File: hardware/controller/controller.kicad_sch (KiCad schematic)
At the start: 0 parts

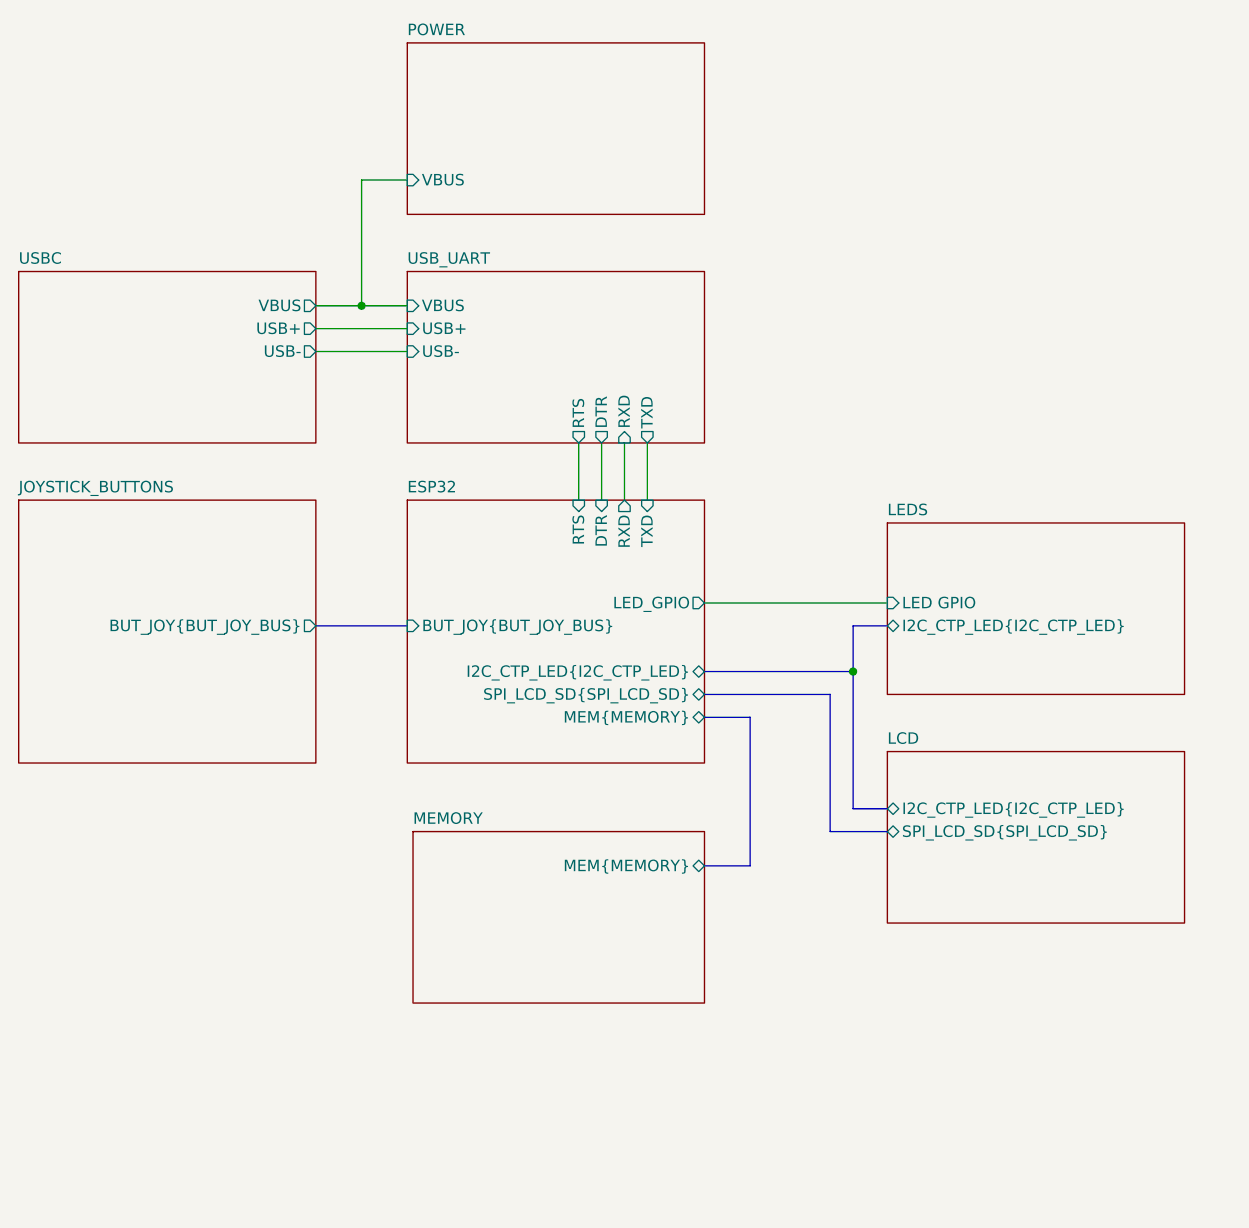
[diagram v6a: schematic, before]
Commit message: modified power circuitry
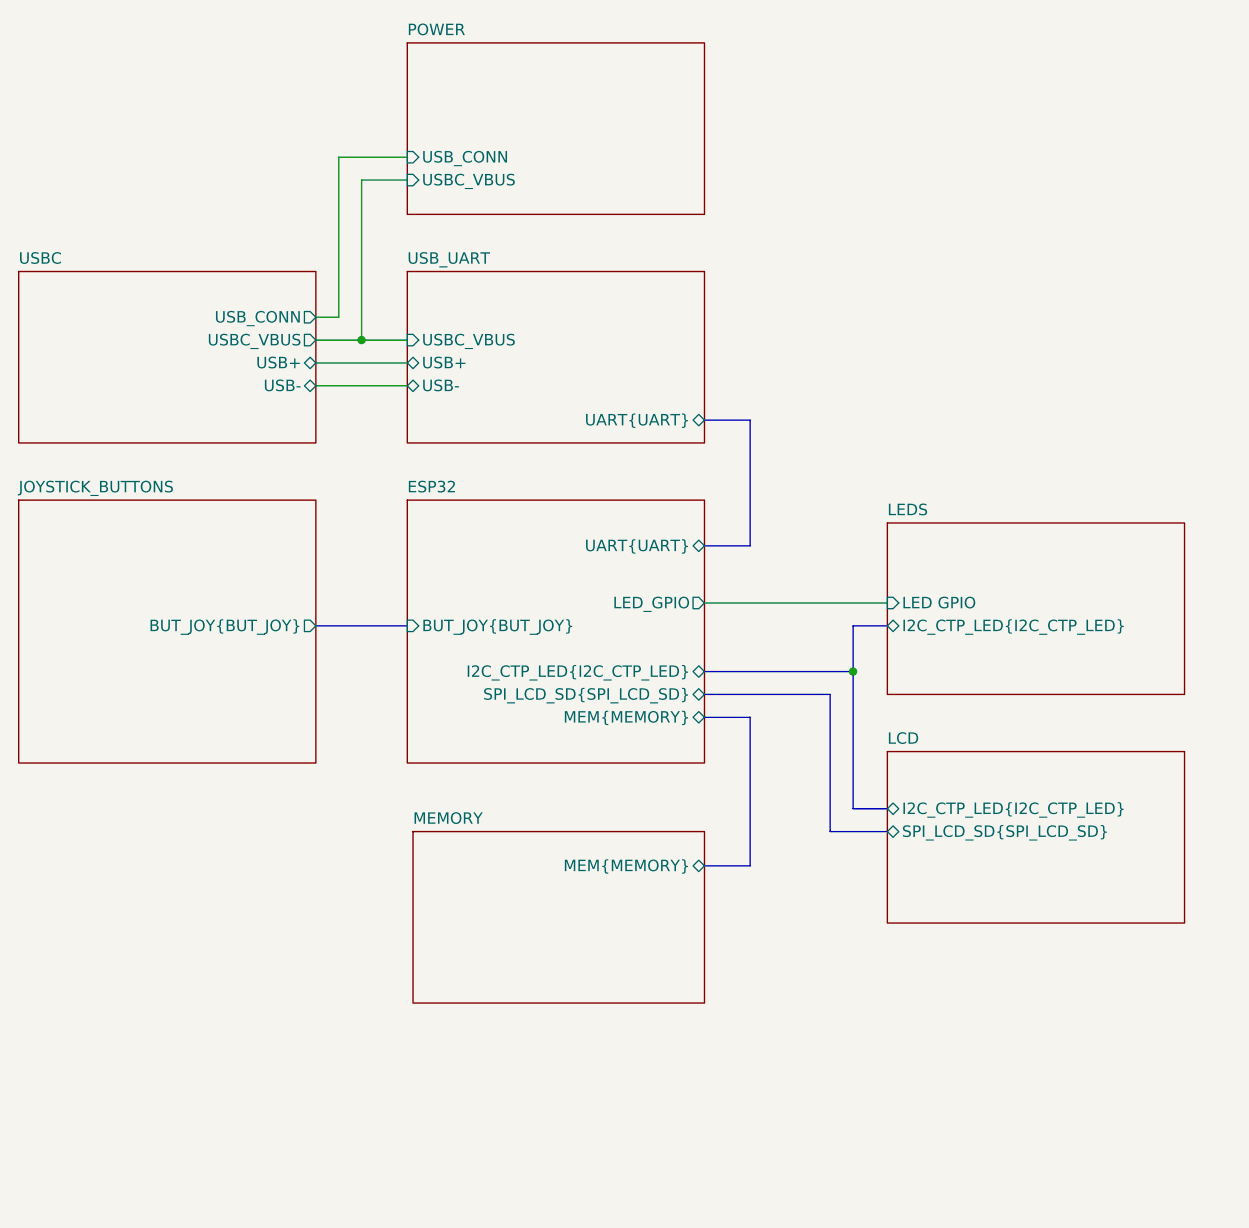
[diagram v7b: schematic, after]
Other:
- sheet ESP32 ports: added BUT_JOY{BUT_JOY}, UART{UART}; removed BUT_JOY{BUT_JOY_BUS}, DTR, RTS, RXD, TXD
- sheet JOYSTICK_BUTTONS ports: added BUT_JOY{BUT_JOY}; removed BUT_JOY{BUT_JOY_BUS}
- sheet POWER ports: added USBC_VBUS, USB_CONN; removed VBUS
- sheet USBC ports: added USBC_VBUS, USB_CONN; removed VBUS
- sheet USB_UART ports: added UART{UART}, USBC_VBUS; removed DTR, RTS, RXD, TXD, VBUS
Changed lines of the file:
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@@
 		(title "Controller")
 	)
-	(bus_alias "BUT_JOY_BUS"
+	(bus_alias "BUT_JOY"
 		(members "JOY1_V" "JOY1_H" "JOY2_V" "JOY2_H" "BUT_LEFT" "BUT_UP" "BUT_DOWN"
 			"BUT_RIGHT" "BUT_BOOT" "BUT_RESET"
@@
 	)
 	(junction
-		(at 96.52 64.77)
+		(at 96.52 68.58)
 		(diameter 0)
 		(color 0 0 0 0)
 	)
+	(wire
+		(pts
+			(xy 91.44 66.04) (xy 93.98 66.04)
+		)
+		(stroke
+			(width 0)
+			(type default)
+		)
+	)
 	(bus
 		(pts
@@
 	(wire
 		(pts
-			(xy 91.44 67.31) (xy 101.6 67.31)
-		)
-		(stroke
-			(width 0)
-			(type default)
-		)
-	)
-	(wire
-		(pts
-			(xy 123.19 80.01) (xy 123.19 86.36)
+			(xy 91.44 71.12) (xy 101.6 71.12)
 		)
 		(stroke
@@
 		)
 	)
+	(wire
+		(pts
+			(xy 93.98 66.04) (xy 93.98 48.26)
+		)
+		(stroke
+			(width 0)
+			(type default)
+		)
+	)
 	(bus
 		(pts
@@
 	(wire
 		(pts
-			(xy 96.52 64.77) (xy 101.6 64.77)
-		)
-		(stroke
-			(width 0)
-			(type default)
-		)
-	)
-	(wire
-		(pts
 			(xy 134.62 97.79) (xy 154.94 97.79)
 		)
@@
 	(bus
 		(pts
+			(xy 139.7 91.44) (xy 134.62 91.44)
+		)
+		(stroke
+			(width 0)
+			(type default)
+		)
+	)
+	(bus
+		(pts
 			(xy 91.44 100.33) (xy 101.6 100.33)
 		)
@@
 		)
 	)
+	(wire
+		(pts
+			(xy 96.52 68.58) (xy 101.6 68.58)
+		)
+		(stroke
+			(width 0)
+			(type default)
+		)
+	)
 	(bus
 		(pts
@@
 	(bus
 		(pts
+			(xy 134.62 77.47) (xy 139.7 77.47)
+		)
+		(stroke
+			(width 0)
+			(type default)
+		)
+	)
+	(bus
+		(pts
 			(xy 134.62 105.41) (xy 151.13 105.41)
 		)
@@
 	(wire
 		(pts
-			(xy 91.44 69.85) (xy 101.6 69.85)
-		)
-		(stroke
-			(width 0)
-			(type default)
-		)
-	)
-	(wire
-		(pts
-			(xy 128.27 80.01) (xy 128.27 86.36)
-		)
-		(stroke
-			(width 0)
-			(type default)
-		)
-	)
-	(wire
-		(pts
-			(xy 96.52 64.77) (xy 96.52 50.8)
+			(xy 91.44 73.66) (xy 101.6 73.66)
+		)
+		(stroke
+			(width 0)
+			(type default)
+		)
+	)
+	(wire
+		(pts
+			(xy 96.52 50.8) (xy 96.52 68.58)
 		)
 		(stroke
@@
 		)
 	)
-	(wire
-		(pts
-			(xy 91.44 64.77) (xy 96.52 64.77)
-		)
-		(stroke
-			(width 0)
-			(type default)
-		)
-	)
-	(wire
-		(pts
-			(xy 120.65 80.01) (xy 120.65 86.36)
-		)
-		(stroke
-			(width 0)
-			(type default)
-		)
-	)
-	(wire
-		(pts
-			(xy 125.73 80.01) (xy 125.73 86.36)
+	(bus
+		(pts
+			(xy 139.7 77.47) (xy 139.7 91.44)
+		)
+		(stroke
+			(width 0)
+			(type default)
+		)
+	)
+	(wire
+		(pts
+			(xy 93.98 48.26) (xy 101.6 48.26)
+		)
+		(stroke
+			(width 0)
+			(type default)
+		)
+	)
+	(wire
+		(pts
+			(xy 91.44 68.58) (xy 96.52 68.58)
 		)
 		(stroke
@@
 			)
 		)
-		(pin "BUT_JOY{BUT_JOY_BUS}" output
+		(pin "BUT_JOY{BUT_JOY}" output
 			(at 91.44 100.33 0)
 			(effects
@@
 			)
 		)
-		(pin "VBUS" output
-			(at 91.44 64.77 0)
-			(effects
-				(font
-					(size 1.27 1.27)
-				)
-				(justify right)
-			)
-		)
-		(pin "USB+" output
-			(at 91.44 67.31 0)
-			(effects
-				(font
-					(size 1.27 1.27)
-				)
-				(justify right)
-			)
-		)
-		(pin "USB-" output
-			(at 91.44 69.85 0)
+		(pin "USBC_VBUS" output
+			(at 91.44 68.58 0)
+			(effects
+				(font
+					(size 1.27 1.27)
+				)
+				(justify right)
+			)
+		)
+		(pin "USB+" bidirectional
+			(at 91.44 71.12 0)
+			(effects
+				(font
+					(size 1.27 1.27)
+				)
+				(justify right)
+			)
+		)
+		(pin "USB-" bidirectional
+			(at 91.44 73.66 0)
+			(effects
+				(font
+					(size 1.27 1.27)
+				)
+				(justify right)
+			)
+		)
+		(pin "USB_CONN" output
+			(at 91.44 66.04 0)
 			(effects
 				(font
@@
 			)
 		)
-		(pin "USB+" input
-			(at 101.6 67.31 180)
-			(effects
-				(font
-					(size 1.27 1.27)
-				)
-				(justify left)
-			)
-		)
-		(pin "USB-" input
-			(at 101.6 69.85 180)
-			(effects
-				(font
-					(size 1.27 1.27)
-				)
-				(justify left)
-			)
-		)
-		(pin "RXD" input
-			(at 125.73 80.01 270)
-			(effects
-				(font
-					(size 1.27 1.27)
-				)
-				(justify left)
-			)
-		)
-		(pin "TXD" output
-			(at 128.27 80.01 270)
-			(effects
-				(font
-					(size 1.27 1.27)
-				)
-				(justify left)
-			)
-		)
-		(pin "RTS" output
-			(at 120.65 80.01 270)
-			(effects
-				(font
-					(size 1.27 1.27)
-				)
-				(justify left)
-			)
-		)
-		(pin "VBUS" input
-			(at 101.6 64.77 180)
-			(effects
-				(font
-					(size 1.27 1.27)
-				)
-				(justify left)
-			)
-		)
-		(pin "DTR" output
-			(at 123.19 80.01 270)
-			(effects
-				(font
-					(size 1.27 1.27)
-				)
-				(justify left)
+		(pin "USB+" bidirectional
+			(at 101.6 71.12 180)
+			(effects
+				(font
+					(size 1.27 1.27)
+				)
+				(justify left)
+			)
+		)
+		(pin "USB-" bidirectional
+			(at 101.6 73.66 180)
+			(effects
+				(font
+					(size 1.27 1.27)
+				)
+				(justify left)
+			)
+		)
+		(pin "USBC_VBUS" input
+			(at 101.6 68.58 180)
+			(effects
+				(font
+					(size 1.27 1.27)
+				)
+				(justify left)
+			)
+		)
+		(pin "UART{UART}" bidirectional
+			(at 134.62 77.47 0)
+			(effects
+				(font
+					(size 1.27 1.27)
+				)
+				(justify right)
 			)
 		)
@@
 			)
 		)
-		(pin "BUT_JOY{BUT_JOY_BUS}" input
+		(pin "BUT_JOY{BUT_JOY}" input
 			(at 101.6 100.33 180)
 			(effects
@@
 				)
 				(justify left)
-			)
-		)
-		(pin "RXD" output
-			(at 125.73 86.36 90)
-			(effects
-				(font
-					(size 1.27 1.27)
-				)
-				(justify right)
-			)
-		)
-		(pin "TXD" input
-			(at 128.27 86.36 90)
-			(effects
-				(font
-					(size 1.27 1.27)
-				)
-				(justify right)
-			)
-		)
-		(pin "RTS" input
-			(at 120.65 86.36 90)
-			(effects
-				(font
-					(size 1.27 1.27)
-				)
-				(justify right)
-			)
-		)
-		(pin "DTR" input
-			(at 123.19 86.36 90)
-			(effects
-				(font
-					(size 1.27 1.27)
-				)
-				(justify right)
 			)
 		)
@@
 		(pin "MEM{MEMORY}" bidirectional
 			(at 134.62 110.49 0)
+			(effects
+				(font
+					(size 1.27 1.27)
+				)
+				(justify right)
+			)
+		)
+		(pin "UART{UART}" bidirectional
+			(at 134.62 91.44 0)
 			(effects
 				(font
@@
 			)
 		)
-		(pin "VBUS" input
+		(pin "USBC_VBUS" input
 			(at 101.6 50.8 180)
 			(effects
 				(font
+					(size 1.27 1.27)
+				)
+				(justify left)
+			)
+		)
+		(pin "USB_CONN" input
+			(at 101.6 48.26 180)
+			(effects
+				(font

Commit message: finished first rev of controller schematic minus actually finding passive components. moved some features to rev2 todo
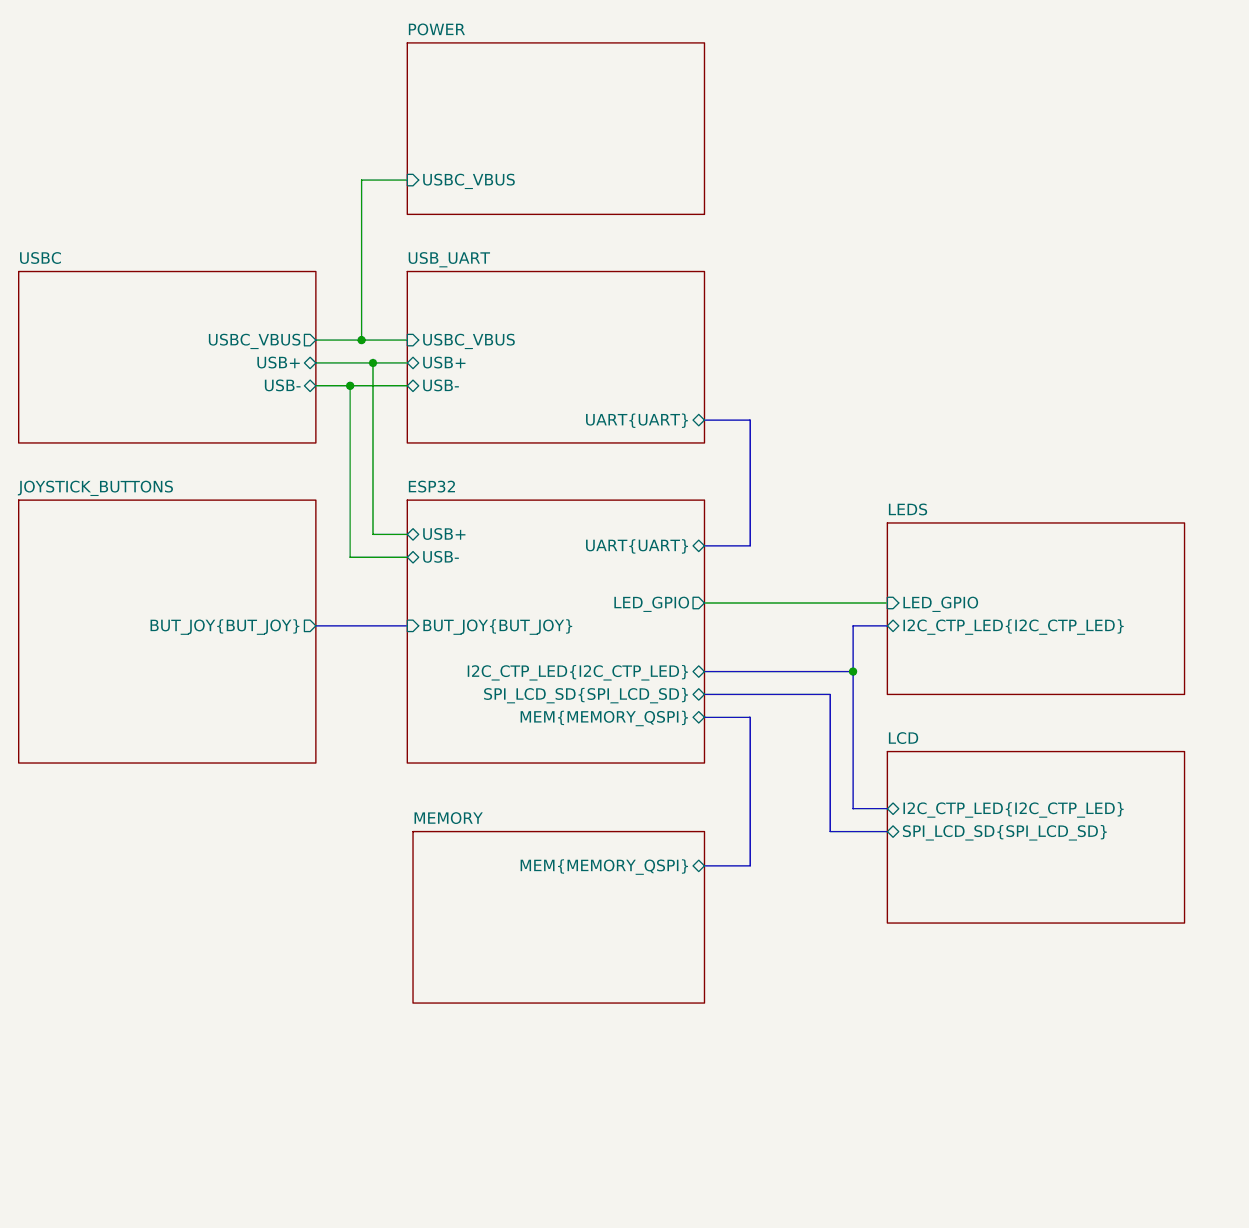
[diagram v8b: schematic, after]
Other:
- sheet ESP32 ports: added MEM{MEMORY_QSPI}, USB+, USB-; removed MEM{MEMORY}
- sheet LEDS ports: added LED_GPIO; removed LED GPIO
- sheet MEMORY ports: added MEM{MEMORY_QSPI}; removed MEM{MEMORY}
- sheet POWER ports: added none; removed USB_CONN
- sheet USBC ports: added none; removed USB_CONN
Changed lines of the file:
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@@
 		(color 0 0 0 0)
 	)
-	(wire
-		(pts
-			(xy 91.44 66.04) (xy 93.98 66.04)
-		)
-		(stroke
-			(width 0)
-			(type default)
-		)
+	(junction
+		(at 97.79 71.12)
+		(diameter 0)
+		(color 0 0 0 0)
+	)
+	(junction
+		(at 95.25 73.66)
+		(diameter 0)
+		(color 0 0 0 0)
 	)
 	(bus
@@
 	(wire
 		(pts
-			(xy 91.44 71.12) (xy 101.6 71.12)
+			(xy 91.44 71.12) (xy 97.79 71.12)
 		)
 		(stroke
@@
 	(wire
 		(pts
-			(xy 93.98 66.04) (xy 93.98 48.26)
+			(xy 95.25 92.71) (xy 101.6 92.71)
 		)
 		(stroke
@@
 	(wire
 		(pts
+			(xy 95.25 73.66) (xy 95.25 92.71)
+		)
+		(stroke
+			(width 0)
+			(type default)
+		)
+	)
+	(wire
+		(pts
 			(xy 134.62 97.79) (xy 154.94 97.79)
 		)
@@
 		)
 	)
+	(wire
+		(pts
+			(xy 97.79 71.12) (xy 101.6 71.12)
+		)
+		(stroke
+			(width 0)
+			(type default)
+		)
+	)
 	(bus
 		(pts
@@
 		)
 	)
+	(wire
+		(pts
+			(xy 95.25 73.66) (xy 101.6 73.66)
+		)
+		(stroke
+			(width 0)
+			(type default)
+		)
+	)
 	(bus
 		(pts
@@
 		)
 	)
+	(wire
+		(pts
+			(xy 97.79 71.12) (xy 97.79 90.17)
+		)
+		(stroke
+			(width 0)
+			(type default)
+		)
+	)
 	(bus
 		(pts
@@
 	(wire
 		(pts
-			(xy 91.44 73.66) (xy 101.6 73.66)
+			(xy 97.79 90.17) (xy 101.6 90.17)
+		)
+		(stroke
+			(width 0)
+			(type default)
+		)
+	)
+	(wire
+		(pts
+			(xy 91.44 73.66) (xy 95.25 73.66)
 		)
 		(stroke
@@
 		(pts
 			(xy 139.7 77.47) (xy 139.7 91.44)
-		)
-		(stroke
-			(width 0)
-			(type default)
-		)
-	)
-	(wire
-		(pts
-			(xy 93.98 48.26) (xy 101.6 48.26)
 		)
 		(stroke
@@
 			)
 		)
-		(pin "MEM{MEMORY}" bidirectional
+		(pin "MEM{MEMORY_QSPI}" bidirectional
 			(at 134.62 127 0)
 			(effects
@@
 			)
 		)
-		(pin "LED GPIO" input
+		(pin "LED_GPIO" input
 			(at 154.94 97.79 180)
 			(effects
@@
 			)
 		)
-		(pin "USB_CONN" output
-			(at 91.44 66.04 0)
-			(effects
-				(font
-					(size 1.27 1.27)
-				)
-				(justify right)
-			)
-		)
 		(instances
 			(project "controller"
@@
 			)
 		)
-		(pin "MEM{MEMORY}" bidirectional
+		(pin "MEM{MEMORY_QSPI}" bidirectional
 			(at 134.62 110.49 0)
 			(effects
@@
 				)
 				(justify right)
+			)
+		)
+		(pin "USB+" bidirectional
+			(at 101.6 90.17 180)
+			(effects
+				(font
+					(size 1.27 1.27)
+				)
+				(justify left)
+			)
+		)
+		(pin "USB-" bidirectional
+			(at 101.6 92.71 180)
+			(effects
+				(font
+					(size 1.27 1.27)
+				)
+				(justify left)
 			)
 		)
@@
 			(effects
 				(font
-					(size 1.27 1.27)
-				)
-				(justify left)
-			)
-		)
-		(pin "USB_CONN" input
-			(at 101.6 48.26 180)
-			(effects
-				(font
